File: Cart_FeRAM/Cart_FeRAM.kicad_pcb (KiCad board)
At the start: 2 copper layers, 83.8 x 52.6 mm, 11 parts, among them CON1 GENESIS-EDGE, J1 Conn_01x32_Male, J2 Conn_01x32_Male, SW1 SW_DIP_x04, U1 74HC74, U2 FM1808B-SG, U3 74LS139, U4 27C322

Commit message: Updated board design, some project clean up
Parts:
- added JP1: <2M/4M, Jumper:SolderJumper-3_P1.3mm_Open_Pad1.0x1.5mm, B.Cu at (123.4, 62.2)
- added R1: 1K, Resistor_THT:R_Axial_DIN0207_L6.3mm_D2.5mm_P7.62mm_Horizontal, F.Cu at (92.6, 91.4)
- added R2: 1K, Resistor_THT:R_Axial_DIN0207_L6.3mm_D2.5mm_P7.62mm_Horizontal, F.Cu at (92.6, 88.4)
- added R3: 1K, Resistor_THT:R_Axial_DIN0207_L6.3mm_D2.5mm_P7.62mm_Horizontal, F.Cu at (92.6, 85.3)
- added R4: 1K, Resistor_THT:R_Axial_DIN0207_L6.3mm_D2.5mm_P7.62mm_Horizontal, F.Cu at (92.6, 73.3)
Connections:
- CON1 pad B6: /A17 -> /CART_A17
- CON1 pad B7: /A18 -> /CART_A18
- CON1 pad B8: /A19 -> /CART_A19
- CON1 pad B9: /A20 -> /CART_A20
- J2 pad 24: /A20 -> /CART_A20
- J2 pad 25: /A19 -> /CART_A19
- J2 pad 26: /A18 -> /CART_A18
- J2 pad 27: /A17 -> /CART_A17
- SW1 pad 1: /A17 -> /CART_A17
- SW1 pad 2: /A18 -> /CART_A18
- SW1 pad 3: /A19 -> /CART_A19
- SW1 pad 4: /A20 -> /CART_A20
- SW1 pad 5: +5V -> /A20
- SW1 pad 6: +5V -> /A19
- SW1 pad 7: +5V -> /A18
- SW1 pad 8: +5V -> /A17
- U1 pad 5: Net-(U1-Pad5) -> Net-(JP1-Pad3)
- U3 pad 2: /A20 -> /CART_A20
- U3 pad 3: Net-(U1-Pad5) -> Net-(JP1-Pad2)
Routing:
- net /CART_A20: track 0.00 -> 119.2 mm, vias 0 -> 1
- net /CART_A17: track 0.00 -> 58.3 mm
- net /CART_A18: track 0.00 -> 58.3 mm
- net /CART_A19: track 0.00 -> 55.8 mm
- net Net-(JP1-Pad3): track 0.00 -> 51.5 mm
- net /A20: track 104.3 -> 72.8 mm, vias 3 -> 0
- net /A8: track 67.3 -> 98.4 mm
- net /A19: track 58.0 -> 27.6 mm, vias 1 -> 0
- net Net-(U1-Pad5): track 26.3 -> 0.00 mm
- net Net-(JP1-Pad2): track 0.00 -> 20.9 mm
- net /A18: track 57.6 -> 39.6 mm
- net /A17: track 67.5 -> 51.0 mm
- net +5V: track 234.6 -> 247.9 mm
- net GND: track 317.8 -> 320.1 mm
- net /D6: track 71.1 -> 72.9 mm
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
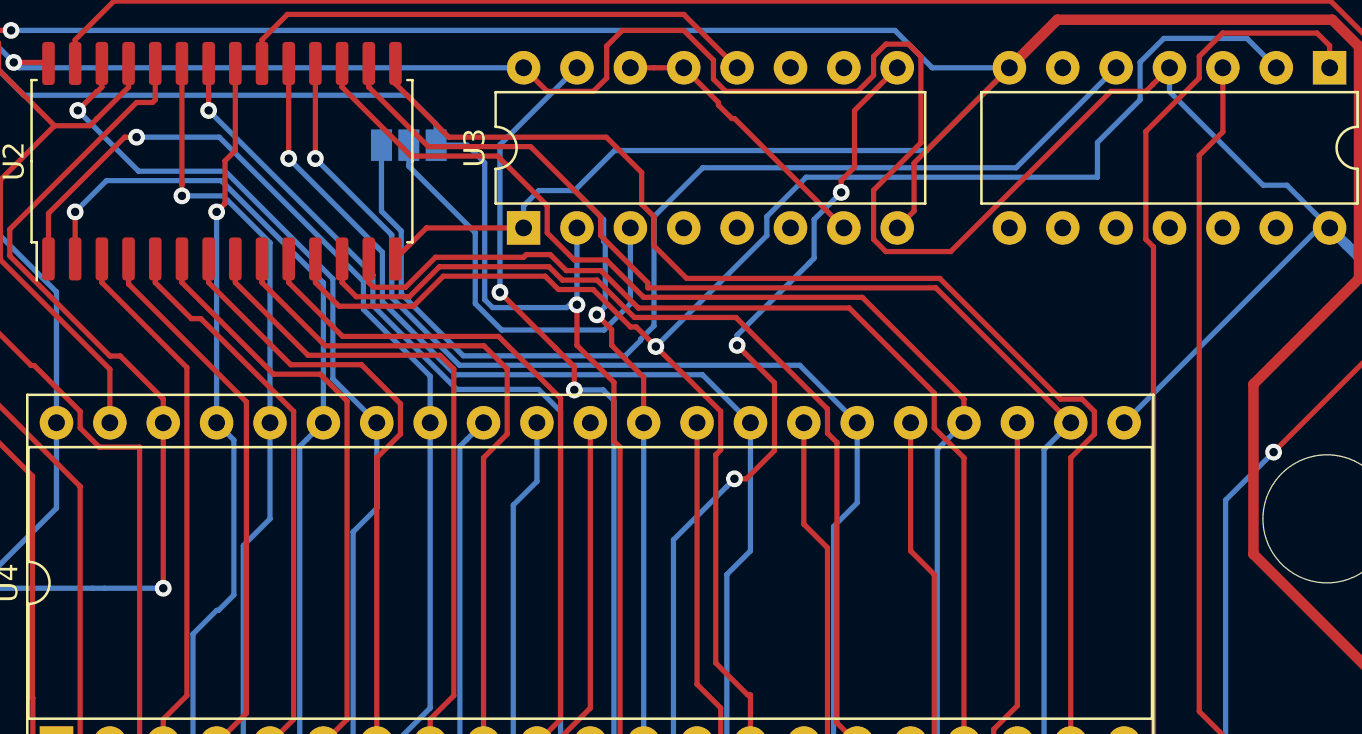
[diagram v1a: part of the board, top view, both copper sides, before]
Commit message: Added IC values to silkscreen, added JP1 identification to silkscreen, added BOM
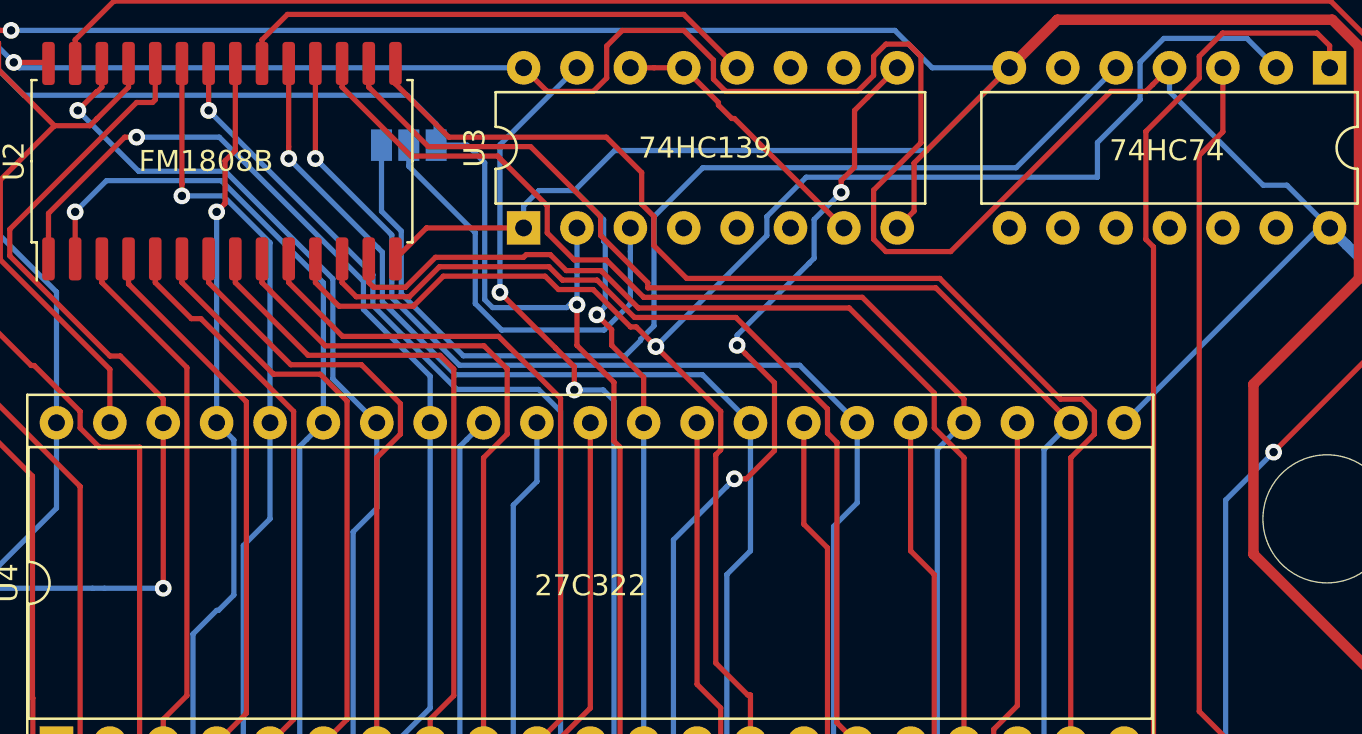
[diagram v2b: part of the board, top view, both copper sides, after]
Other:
- board text added: "27C322"
- board text added: "74HC139"
- board text added: "74HC74"
- board text added: "<2MB"
- board text added: ">2MB"
- board text added: "FM1808B"
- board text added: "ROM SIZE"
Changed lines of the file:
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@@
   (general
     (thickness 1.6)
-    (drawings 8)
+    (drawings 15)
     (tracks 917)
     (zones 0)
@@
   (page A4)
   (layers
-    (0 F.Cu signal)
+    (0 F.Cu signal hide)
     (31 B.Cu signal)
     (32 B.Adhes user)
@@
     )
   )
+  (gr_text ">2MB\n" (at 118.872 62.23) (layer B.SilkS)
+    (effects (font (size 1 1) (thickness 0.15)) (justify mirror))
+  )
+  (gr_text "<2MB\n" (at 128.143 62.357) (layer B.SilkS)
+    (effects (font (size 1 1) (thickness 0.15)) (justify mirror))
+  )
+  (gr_text "ROM SIZE" (at 123.571 64.516) (layer B.SilkS)
+    (effects (font (size 1 1) (thickness 0.15)) (justify mirror))
+  )
+  (gr_text 74HC74 (at 159.512 62.484) (layer F.SilkS)
+    (effects (font (size 1 1) (thickness 0.15)))
+  )
+  (gr_text 74HC139 (at 137.541 62.357) (layer F.SilkS)
+    (effects (font (size 1 1) (thickness 0.15)))
+  )
+  (gr_text FM1808B (at 113.792 62.992) (layer F.SilkS)
+    (effects (font (size 1 1) (thickness 0.15)))
+  )
+  (gr_text 27C322 (at 132.08 83.185) (layer F.SilkS)
+    (effects (font (size 1 1) (thickness 0.15)))
+  )
   (gr_text B1 (at 92.075 105.029) (layer F.SilkS)
     (effects (font (size 0.7 0.7) (thickness 0.1)))
@@
   (segment (start 109.71637 72.263) (end 109.223232 72.263) (width 0.25) (layer F.Cu) (net 5))
   (segment (start 104.4575 66.2305) (end 110.49 60.198) (width 0.25) (layer F.Cu) (net 5))
-  (segment (start 104.775001 104.228003) (end 104.775001 109.728) (width 0.25) (layer F.Cu) (net 78))
-  (segment (start 103.632 99.822) (end 103.632 103.085002) (width 0.25) (layer F.Cu) (net 78))
-  (segment (start 103.632 103.085002) (end 104.775001 104.228003) (width 0.25) (layer F.Cu) (net 78))
   (segment (start 109.22 90.678) (end 109.22 93.65699) (width 0.25) (layer B.Cu) (net 6))
   (segment (start 109.22 93.65699) (end 108.89699 93.98) (width 0.25) (layer B.Cu) (net 6))
@@
   (segment (start 94.416999 78.557001) (end 98.138989 74.835011) (width 0.25) (layer B.Cu) (net 6))
   (segment (start 98.138989 74.835011) (end 98.138989 60.738011) (width 0.25) (layer B.Cu) (net 6))
-  (segment (start 107.315001 109.728) (end 107.315001 105.283001) (width 0.25) (layer F.Cu) (net 79))
-  (segment (start 106.172 104.14) (end 106.172 99.822) (width 0.25) (layer F.Cu) (net 79))
-  (segment (start 107.315001 105.283001) (end 106.172 104.14) (width 0.25) (layer F.Cu) (net 79))
   (segment (start 102.489 90.678) (end 100.203 88.392) (width 0.25) (layer B.Cu) (net 7))
   (segment (start 106.68 90.678) (end 102.489 90.678) (width 0.25) (layer B.Cu) (net 7))
@@
   (segment (start 100.424001 70.452001) (end 101.346 71.374) (width 0.25) (layer B.Cu) (net 7))
   (segment (start 101.346 73.025) (end 101.328001 73.042999) (width 0.25) (layer B.Cu) (net 7))
-  (segment (start 108.806999 101.11908) (end 108.806999 103.980999) (width 0.25) (layer F.Cu) (net 80))
-  (segment (start 108.712 99.822) (end 108.712 101.024081) (width 0.25) (layer F.Cu) (net 80))
-  (segment (start 108.712 101.024081) (end 108.806999 101.11908) (width 0.25) (layer F.Cu) (net 80))
-  (segment (start 109.855001 105.029001) (end 109.855001 109.728) (width 0.25) (layer F.Cu) (net 80))
-  (segment (start 108.806999 103.980999) (end 109.855001 105.029001) (width 0.25) (layer F.Cu) (net 80))
   (segment (start 106.68 69.215) (end 100.711 63.246) (width 0.25) (layer B.Cu) (net 8))
   (segment (start 106.68 75.438) (end 106.68 69.215) (width 0.25) (layer B.Cu) (net 8))
@@
   (segment (start 106.68 79.502) (end 106.68 75.438) (width 0.25) (layer B.Cu) (net 8))
   (segment (start 101.637999 84.544001) (end 106.68 79.502) (width 0.25) (layer B.Cu) (net 8))
-  (segment (start 112.395001 109.728) (end 112.395001 105.029001) (width 0.25) (layer F.Cu) (net 81))
-  (segment (start 111.252 103.886) (end 111.252 99.822) (width 0.25) (layer F.Cu) (net 81))
-  (segment (start 112.395001 105.029001) (end 111.252 103.886) (width 0.25) (layer F.Cu) (net 81))
-  (segment (start 127.054998 69.581) (end 127.054998 63.064002) (width 0.25) (layer B.Cu) (net 81))
-  (segment (start 127.431998 69.958) (end 127.054998 69.581) (width 0.25) (layer B.Cu) (net 81))
-  (segment (start 130.956 69.958) (end 127.431998 69.958) (width 0.25) (layer B.Cu) (net 81))
-  (segment (start 131.445 69.469) (end 130.956 69.958) (width 0.25) (layer B.Cu) (net 81))
-  (segment (start 131.445 69.469) (end 131.445 66.167) (width 0.25) (layer B.Cu) (net 81))
-  (segment (start 126.220996 62.23) (end 124.744 62.23) (width 0.25) (layer B.Cu) (net 81))
-  (segment (start 127.054998 63.064002) (end 126.220996 62.23) (width 0.25) (layer B.Cu) (net 81))
-  (via (at 131.445 69.824019) (size 0.8) (drill 0.4) (layers F.Cu B.Cu) (net 81))
-  (segment (start 131.445 69.469) (end 131.445 69.824019) (width 0.25) (layer B.Cu) (net 81))
   (segment (start 130.665001 91.218001) (end 128.919002 92.964) (width 0.25) (layer F.Cu) (net 9))
   (segment (start 130.665001 90.427997) (end 130.665001 91.218001) (width 0.25) (layer F.Cu) (net 9))
@@
   (segment (start 135.110001 70.826997) (end 134.4735 71.463498) (width 0.25) (layer B.Cu) (net 77))
   (segment (start 134.4735 71.463498) (end 134.4735 71.5205) (width 0.25) (layer B.Cu) (net 77))
+  (segment (start 104.775001 104.228003) (end 104.775001 109.728) (width 0.25) (layer F.Cu) (net 78))
+  (segment (start 103.632 99.822) (end 103.632 103.085002) (width 0.25) (layer F.Cu) (net 78))
+  (segment (start 103.632 103.085002) (end 104.775001 104.228003) (width 0.25) (layer F.Cu) (net 78))
   (segment (start 103.632 79.645822) (end 103.632 99.822) (width 0.25) (layer F.Cu) (net 78))
   (segment (start 91.51599 67.529812) (end 103.632 79.645822) (width 0.25) (layer F.Cu) (net 78))
@@
   (segment (start 93.091 58.166) (end 92.041 58.166) (width 0.25) (layer F.Cu) (net 78))
   (segment (start 92.041 58.166) (end 91.51599 58.69101) (width 0.25) (layer F.Cu) (net 78))
+  (segment (start 107.315001 109.728) (end 107.315001 105.283001) (width 0.25) (layer F.Cu) (net 79))
+  (segment (start 106.172 104.14) (end 106.172 99.822) (width 0.25) (layer F.Cu) (net 79))
+  (segment (start 107.315001 105.283001) (end 106.172 104.14) (width 0.25) (layer F.Cu) (net 79))
   (segment (start 107.021999 98.972001) (end 107.021999 93.305999) (width 0.25) (layer F.Cu) (net 79))
   (segment (start 106.172 99.822) (end 107.021999 98.972001) (width 0.25) (layer F.Cu) (net 79))
@@
   (segment (start 99.494597 74.872009) (end 91.965999 67.343411) (width 0.25) (layer F.Cu) (net 79))
   (segment (start 102.43101 74.87201) (end 99.494597 74.872009) (width 0.25) (layer F.Cu) (net 79))
+  (segment (start 108.806999 101.11908) (end 108.806999 103.980999) (width 0.25) (layer F.Cu) (net 80))
+  (segment (start 108.712 99.822) (end 108.712 101.024081) (width 0.25) (layer F.Cu) (net 80))
+  (segment (start 108.712 101.024081) (end 108.806999 101.11908) (width 0.25) (layer F.Cu) (net 80))
+  (segment (start 109.855001 105.029001) (end 109.855001 109.728) (width 0.25) (layer F.Cu) (net 80))
+  (segment (start 108.806999 103.980999) (end 109.855001 105.029001) (width 0.25) (layer F.Cu) (net 80))
   (segment (start 108.712 94.996) (end 108.712 99.822) (width 0.25) (layer F.Cu) (net 80))
   (segment (start 107.805001 94.089001) (end 108.712 94.996) (width 0.25) (layer F.Cu) (net 80))
@@
   (segment (start 99.680998 74.422) (end 103.759 74.422) (width 0.25) (layer F.Cu) (net 80))
   (segment (start 103.759 74.422) (end 107.805001 78.468001) (width 0.25) (layer F.Cu) (net 80))
+  (segment (start 112.395001 109.728) (end 112.395001 105.029001) (width 0.25) (layer F.Cu) (net 81))
+  (segment (start 111.252 103.886) (end 111.252 99.822) (width 0.25) (layer F.Cu) (net 81))
+  (segment (start 112.395001 105.029001) (end 111.252 103.886) (width 0.25) (layer F.Cu) (net 81))
+  (segment (start 127.054998 69.581) (end 127.054998 63.064002) (width 0.25) (layer B.Cu) (net 81))
+  (segment (start 127.431998 69.958) (end 127.054998 69.581) (width 0.25) (layer B.Cu) (net 81))
+  (segment (start 130.956 69.958) (end 127.431998 69.958) (width 0.25) (layer B.Cu) (net 81))
+  (segment (start 131.445 69.469) (end 130.956 69.958) (width 0.25) (layer B.Cu) (net 81))
+  (segment (start 131.445 69.469) (end 131.445 66.167) (width 0.25) (layer B.Cu) (net 81))
+  (segment (start 126.220996 62.23) (end 124.744 62.23) (width 0.25) (layer B.Cu) (net 81))
+  (segment (start 127.054998 63.064002) (end 126.220996 62.23) (width 0.25) (layer B.Cu) (net 81))
+  (via (at 131.445 69.824019) (size 0.8) (drill 0.4) (layers F.Cu B.Cu) (net 81))
+  (segment (start 131.445 69.469) (end 131.445 69.824019) (width 0.25) (layer B.Cu) (net 81))
   (segment (start 94.22237 65.786) (end 94.47637 66.04) (width 0.25) (layer B.Cu) (net 81))
   (segment (start 93.091 65.786) (end 94.22237 65.786) (width 0.25) (layer B.Cu) (net 81))
